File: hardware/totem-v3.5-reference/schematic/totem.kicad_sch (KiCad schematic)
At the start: 136 parts, among them J1 USB_C_Receptacle_USB2.0_16P, J2 LiPo 1000mAh, J3 u.FL, Q1 AO3401A, Q2 2N7002, Q3 2N7002, Q4 AO3401A, Q5 2N7002, SW1 power, SW2 SOS, U1 ESP32-WROOM-32E, U2 MAX-M10S, U3 TP4056-42-ESOP8, U4 AP2112K-3.3, U5 ICM-20948

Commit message: measure: the outline and part positions from the reference board's photos
A single px-per-mm figure was up to 4% off across the radio-side photo,
which has visible perspective. It is now mapped to the board plane by a
homography fitted to the ESP32's and MAX-M10S's castellated pads (38 +
18, known pitch), and the outline is traced from the photo's own edge,
stretch by stretch, at each edge's measured angle.

The LED-side photo turned out to be a quarter-turned view from below; it
is registered by edges clean from that side and gives the ring (centre
(-2.02, 2.45), R 18.24 mm, LEDs every 6 degrees), the crystal cluster,
the IMU and the microphone. The two photos disagree by ~1.3 mm on the
right side; README.md states it and asks for calipers there.

What the photos also showed, now in the schematic:
- the buttons are top-actuated 6x6 SMD tact switches (PTS645 land
  pattern), not side-actuated; the custom footprint is gone
- resistors are 0603 and bulk capacitors 0805 on the reference board
- the touch post sits under the ESP32 module, so its pad is SMD

Claude-Session: https://claude.ai/code/session_0192KwQN6XkBBxwoQn8x3FMV
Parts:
- C1, C12, C18, C2, C4, C6, C7, C8: footprint Capacitor_SMD:C_0402_1005Metric -> Capacitor_SMD:C_0603_1608Metric
- C10, C11, C13, C14, C15, C16, C17, C3, C5: footprint Capacitor_SMD:C_0603_1608Metric -> Capacitor_SMD:C_0805_2012Metric
- R1, R10, R11, R12, R13, R14, R15, R16, R17, R18, R19, R2, R20, R21, R22, R23, R24, R25, R26, R3, R4, R5, R6, R7, R8, R9: footprint Resistor_SMD:R_0402_1005Metric -> Resistor_SMD:R_0603_1608Metric
- SW1, SW2: footprint totem:SW_Side_6x6 -> Button_Switch_SMD:SW_SPST_PTS645Sx43SMTR92
- TP1: footprint TestPoint:TestPoint_THTPad_D2.0mm_Drill1.0mm -> TestPoint:TestPoint_Pad_D2.5mm

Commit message: fix: the ring is 1515 LEDs, measured, and the sim draws their real current
The ring's packages measure 1.50 mm wide at a 1.91 mm pitch; sixty
2 mm WS2812B-2020s cannot fit that circle. The footprint is drawn from
the XL-1515RGBC-WS2812B datasheet's land pattern; its pins are numbered
as the 2020's, so the symbol stays.

At the datasheet's 5 mA per channel, full white now holds the rail above
3.0 V at the lowest full-feature cell, so it is a check, not a known
limit. The one known limit left is VLED against the 1515's 3.5 V floor
on a 3.45 V cell, which the reference board shares.

Claude-Session: https://claude.ai/code/session_0192KwQN6XkBBxwoQn8x3FMV
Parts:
- D100, D101, D102, D103, D104, D105, D106, D107, D108, D109, D110, D111, D112, D113, D114, D115, D116, D117, D118, D119, D120, D121, D122, D123, D124, D125, D126, D127, D128, D129, D130, D131, D132, D133, D134, D135, D136, D137, D138, D139, D140, D141, D142, D143, D144, D145, D146, D147, D148, D149, D150, D151, D152, D153, D154, D155, D156, D157, D158, D159, D200, D201, D202, D203, D204, D205, D206: value WS2812B-2020 -> XL-1515RGBC-WS2812B; footprint LED_SMD:LED_WS2812B-2020_PLCC4_2.0x2.0mm -> totem:LED_XL-1515RGBC-WS2812B

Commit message: feat: the board placed from the photos, with planes and rules
build.py makes schematic/totem.kicad_pcb from the schematic's netlist
and the measured outline and positions: 136 parts, the ring and crystal
oriented so DI/VDD face out and DO faces the next LED, the IMU with pin 1
where its marking puts it. In1 is GND, In2 3V3 with a VLED bridge across
the ring band; on the LED side a VLED pour outside the ring and a GND
pour inside feed the ring's pads.

The USB-C is now a power-only, all-SMD GCT USB4135: a 16-pin part's rear
shell tabs would land on the ring (usbfit.py tried every USB-C in the
library). Placement DRC: no shorts, clearance or edge errors; two
courtyard overlaps the photos show (TP4056 by the module, SOS LED
between the switch's legs) are left for documented exclusions.

Claude-Session: https://claude.ai/code/session_0192KwQN6XkBBxwoQn8x3FMV
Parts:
- J1: value USB_C_Receptacle_USB2.0_16P -> USB4135-GF-A; footprint Connector_USB:USB_C_Receptacle_HRO_TYPE-C-31-M-12 -> Connector_USB:USB_C_Receptacle_GCT_USB4135-GF-A_6P_TopMnt_Horizontal; symbol Connector:USB_C_Receptacle_USB2.0_16P -> Connector:USB_C_Receptacle_PowerOnly_6P
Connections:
- net GND: no longer J1.A1 (GND), J1.B1 (GND)
- net VBUS: no longer J1.A4 (VBUS), J1.B4 (VBUS)
- no-connect marks 53 -> 47

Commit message: feat: the board routed, DRC clean on every electrical check
route.py is a grid A* router over F.Cu and B.Cu with KiCad's own pad
polygons, per-class clearances from distance transforms, footprint rule
areas, and PathFinder-style history cost on rip-up; it converges to
every net routed, then checks connectivity itself. The LED side's VLED
pour is kept whole by a band no other net may cross; the one crossing
the ring's data needs (D100's DI faces out) is matched by feeding VLED
to D159 on the far side. The microphone uses a gapped GND ring
(mic_footprint.py) so its signal leaves on its own layer.

kicad-cli DRC: 0 unconnected, 0 clearance, 0 shorts, 0 narrow
connections, 0 keepout violations. Left: silkscreen warnings, the two
courtyard overlaps the photos show, and library-mismatch notes.

Docs: U5 and 'U6 I2948' were one chip seen from two angles; J1 carries
no data; the ring's LEDs are 1515s.

Claude-Session: https://claude.ai/code/session_0192KwQN6XkBBxwoQn8x3FMV
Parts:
- MK1: footprint Sensor_Audio:CUI_CMC-4013-SMT -> totem:CUI_CMC-4013-SMT_RingGap

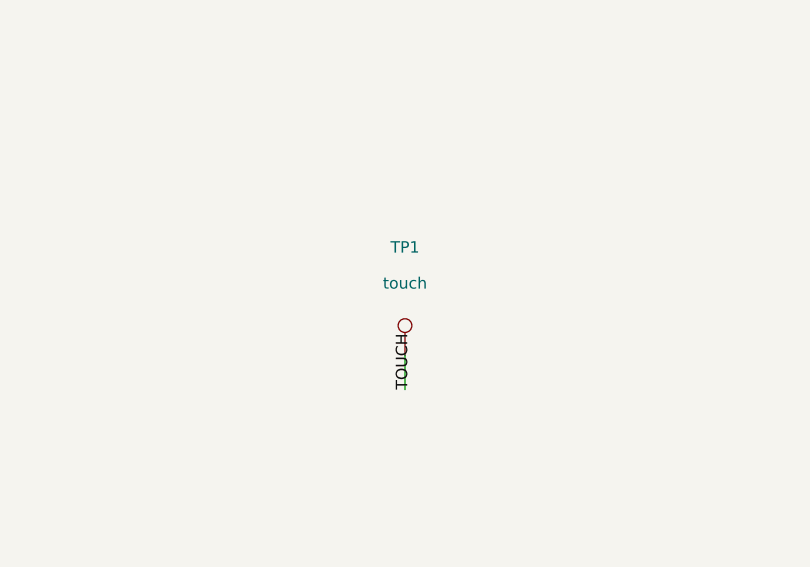
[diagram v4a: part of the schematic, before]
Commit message: fix: DRC clean with schematic parity, every check at every severity
- the LED footprint's pin mark moves to the ring's inner edge by DO, where
  the datasheet puts it and no neighbour's pad is
- references come off the silkscreen (0.3-0.4 mm between parts leaves no
  room); the fab layers and placement file keep them
- the gapped microphone footprint drops a silk circle that ran off the edge
- the three overlaps the reference board has (TP4056 by the module, SOS
  LED between the switch's legs) are narrow custom rules in
  totem.kicad_dru, each with its reason
- programming pads leave the BOM; the touch post's spring stays in it,
  and its comment now says what the photos show: an SMD spring, not a hole

kicad-cli pcb drc --schematic-parity --severity-all: 0 violations,
0 unconnected, 0 footprint errors. ERC 0/0.

Claude-Session: https://claude.ai/code/session_0192KwQN6XkBBxwoQn8x3FMV
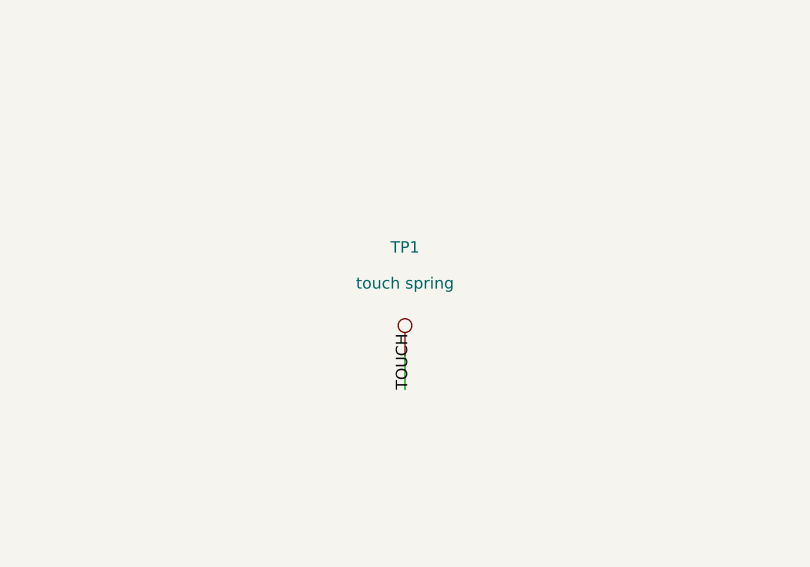
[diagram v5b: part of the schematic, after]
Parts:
- TP1: value touch -> touch spring
- TP2, TP3, TP4, TP5, TP6, TP7: now left out of the parts list

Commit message: hardware: ST motion sensors, the LED side's missing parts, and a BOM of parts that exist (#12)
Close-up photographs of the reference board's LED side, and a
part-by-part check of the BOM against DigiKey and LCSC, changed the
board.

## LED side: what the close-ups showed

| Reference board | Before this PR | Now |
| --- | --- | --- |
| **Two 0603 LEDs** in the crystal below the touch post, each with an
0603 resistor | Missing; the TP4056's `CHRG`/`STDBY` were left open | D4
(red, charging) and D5 (green, charged) with 1k each, at the
photographed positions. Colours aren't visible unlit; red/green is the
TP4056 convention |
| **Through-hole JST**: its pins' joints show on the LED side, 1.96 mm
apart | SMD JST, 2 mm further in | **S2B-PH-K-S** on the measured pins,
overhanging the corner like the original |
| **Gold SMT pogo pin** as the touch post | Called a "conical spring" |
Same pad; BOM and assembly notes corrected |
| **THT-shell USB-C**: four plated slots at ±4.80 mm, rows 3.0 mm apart,
two holes 6.5 mm apart | USB4135 (SMD) | Unchanged: no catalogue
footprint checked matches that pattern (HRO, GCT USB4105/USB4125, SHOU
HAN 6P and recessed 6P). Recorded in the README with the measurements |
| ~25 small parts in the cluster below the crystal, ~8 in a column by
the ring | This design's own circuit does those jobs | Unchanged;
documented as photographed, not copied. Values and nets can't be read |

## Motion sensing: ST LSM6DSV16X + LIS2MDL

The ICM-20948 is obsolete (DigiKey: "no longer manufactured"). The
LSM6DSV16X sits on its site and the LIS2MDL beside it. Both are on I2C0,
wired to ST's application circuits (DS13510 Fig. 28, DS12144 Fig. 5),
with data-ready lines to IO32/IO33.

From the datasheets, typical values:

| | ICM-20948 | LSM6DSV16X + LIS2MDL |
| --- | --- | --- |
| Gyro noise density | 0.015 dps/√Hz | 0.0028 dps/√Hz |
| Gyro zero-rate drift over temperature | ±0.05 dps/°C | ±0.006 dps/°C |
| Accelerometer noise density | 230 µg/√Hz | 60 µg/√Hz |
| 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
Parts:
- added C19, C21: 100n, Capacitor_SMD:C_0603_1608Metric, symbol Device:C
- added C20: 10u, Capacitor_SMD:C_0805_2012Metric, symbol Device:C
- added D4: red, LED_SMD:LED_0603_1608Metric, symbol Device:LED
- added D5: green, LED_SMD:LED_0603_1608Metric, symbol Device:LED
- added R27, R28: 1k, Resistor_SMD:R_0603_1608Metric, symbol Device:R
- added U6: LIS2MDL, Package_LGA:LGA-12_2x2mm_P0.5mm, symbol Sensor_Magnetic:LIS2MDL
- C8: value 100n -> 220n
- J2: footprint Connector_JST:JST_PH_S2B-PH-SM4-TB_1x02-1MP_P2.00mm_Horizontal -> Connector_JST:JST_PH_S2B-PH-K_1x02_P2.00mm_Horizontal
- R1: value 120k -> 113k
- R2: value 108k -> 102k
- TP1: value touch spring -> touch pogo pin
- U5: value ICM-20948 -> LSM6DSV16X; footprint Sensor_Motion:InvenSense_QFN-24_3x3mm_P0.4mm -> Package_LGA:LGA-14_3x2.5mm_P0.5mm_LayoutBorder3x4y; symbol Sensor_Motion:ICM-20948 -> Sensor_Motion:LSM6DSM
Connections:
- net +3V3: now also C1.1, U5.12 (CS), U5.5 (VDDIO), C19.1, C20.1, C21.1, U6.10 (Vdd_IO), U6.3 (~{CS}), U6.9 (Vdd); no longer C8.1, U5.13 (VDD), U5.22 (~{CS})
- net GND: now also U5.6 (GND), U5.7 (GND), C19.2, C20.2, C21.2, U6.6 (GND), U6.8 (GND); no longer U5.18 (GND), U5.20 (GND)
- net I2C0_SCL: now also U5.13 (SCL), U6.1 (SCL/SPC); no longer U5.23 (SCL/SCLK)
- net I2C0_SDA: now also U5.14 (SDA), U6.4 (SDA/SDI/SDO); no longer U5.24 (SDA/SDI)
- net VBUS: now also R27.1, R28.1
- net STDBY: now reaches U3.6 (~{STDBY})
- net STDBY: now also D5.1 (K)
- net CHRG: now reaches U3.7 (~{CHRG})
- net CHRG: now also D4.1 (K)
- net IMU_SA0: now reaches U5.1 (SDO/SA0)
- net IMU_SA0: now also R26.1, U5.2 (SDX), U5.3 (SCX)
- net IMU_INT1: now reaches U5.4 (INT1)
- net IMU_INT1: now also U1.8 (IO32)
- net MAG_DRDY: now reaches U1.9 (IO33)
- net MAG_DRDY: now also U6.7 (DRDY)
- net IMU_AD0: no longer names the net of U5.9 (INT2)
- net IMU_AD0: no longer R26.1
- net REGOUT: no longer names the net of U5.10 (OCS_Aux)
- net REGOUT: no longer C1.1
- new net: D5.2 (A), R28.2
- new net: D4.2 (A), R27.2
- new net MAG_C1: C8.1, U6.5 (C1)
- no-connect marks 47 -> 34
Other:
- moved on the sheet: C1, C7, C8, R26, R7, R8
